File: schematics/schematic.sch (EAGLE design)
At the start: 8 parts, among them IC1 4021N, IC2 4021N

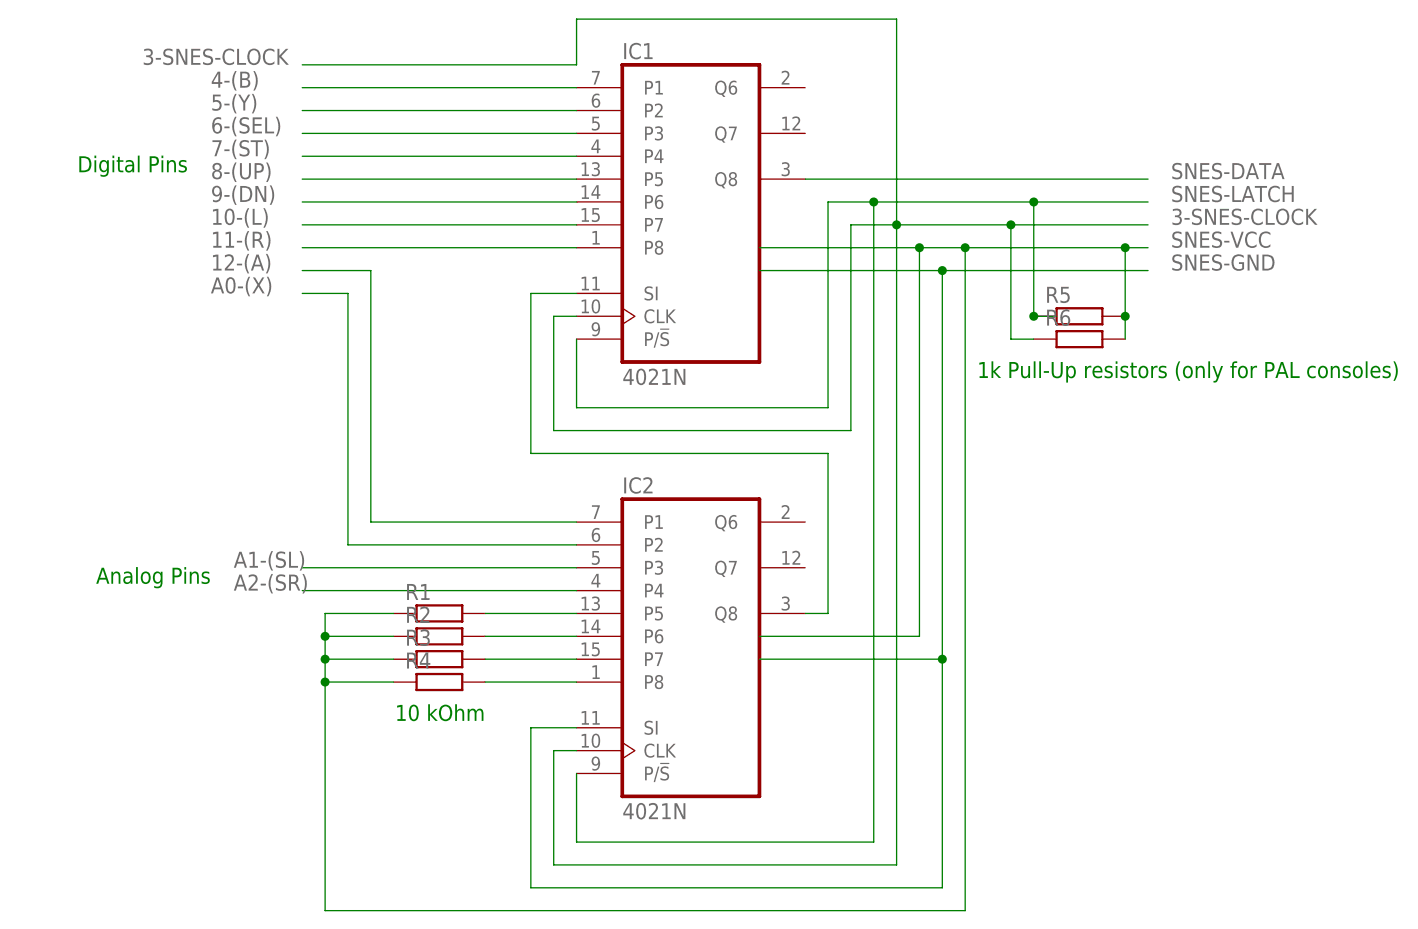
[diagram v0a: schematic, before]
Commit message: Updated schematic - connect latch to arduino
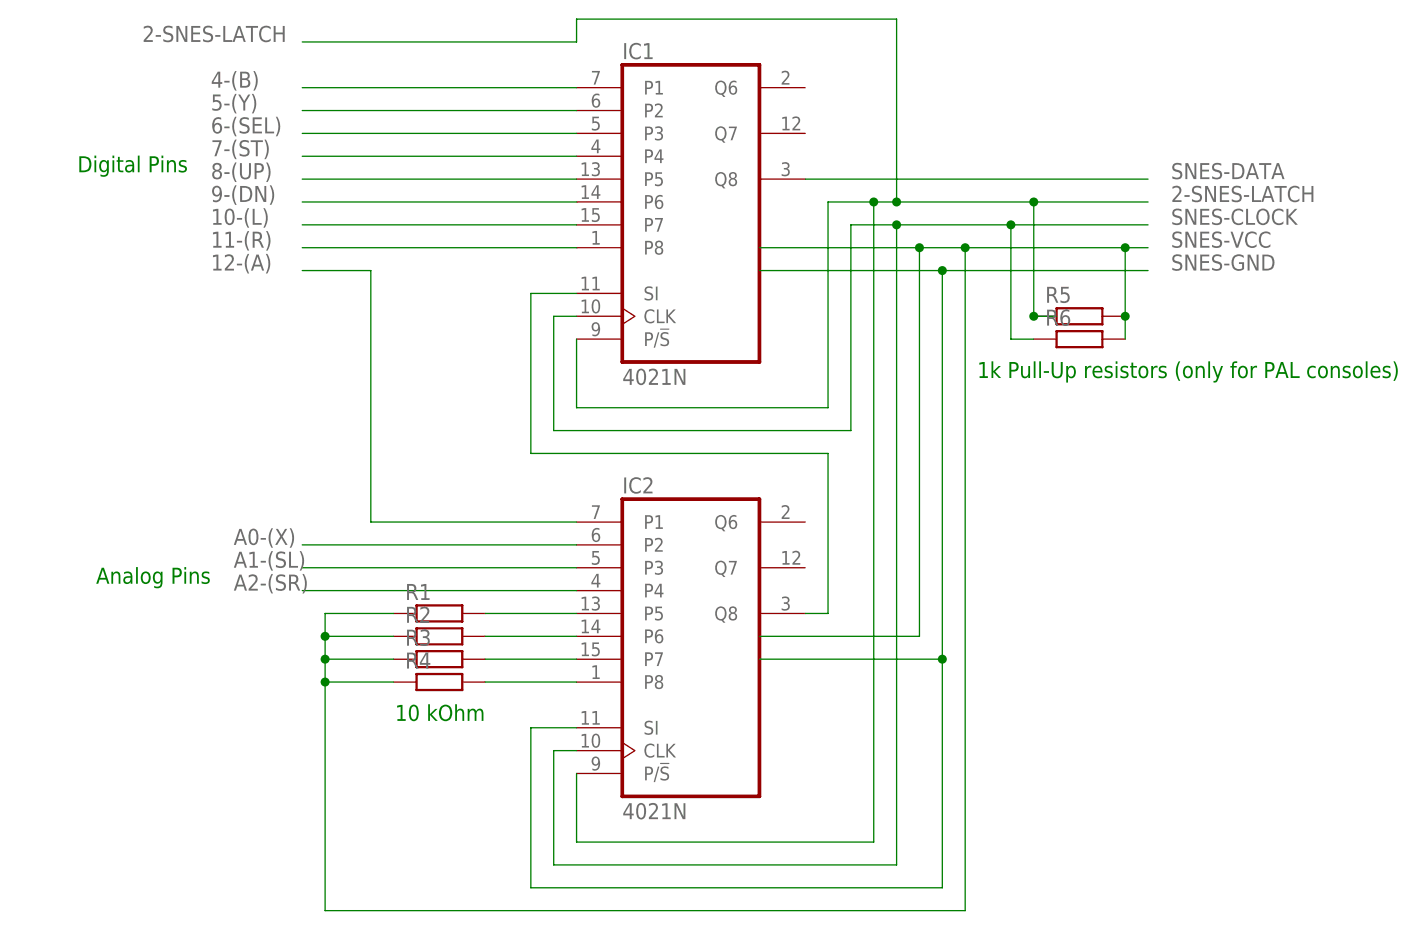
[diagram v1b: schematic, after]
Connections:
- net 3-SNES-CLOCK renamed SNES-CLOCK
- net SNES-LATCH renamed 2-SNES-LATCH
- new net A0-(X): IC2A.P2
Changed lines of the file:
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@@
-</segment>
-</net>
-<net name="A0-(X)" class="0">
-<segment>
-<wire x1="48.26" y1="30.48" x2="22.86" y2="30.48" width="0.1524" layer="91"/>
-<wire x1="22.86" y1="30.48" x2="22.86" y2="58.42" width="0.1524" layer="91"/>
-<wire x1="22.86" y1="58.42" x2="17.78" y2="58.42" width="0.1524" layer="91"/>
-<label x="7.62" y="58.42" size="1.778" layer="95"/>
 </segment>
 </net>
@@
 </segment>
 </net>
-<net name="SNES-LATCH" class="0">
+<net name="2-SNES-LATCH" class="0">
 <segment>
 <pinref part="IC1" gate="A" pin="P/!S"/>
@@
 <label x="114.3" y="68.58" size="1.778" layer="95"/>
 <pinref part="IC2" gate="A" pin="P/!S"/>
-<wire x1="81.28" y1="68.58" x2="99.06" y2="68.58" width="0.1524" layer="91"/>
+<wire x1="81.28" y1="68.58" x2="83.82" y2="68.58" width="0.1524" layer="91"/>
+<wire x1="83.82" y1="68.58" x2="99.06" y2="68.58" width="0.1524" layer="91"/>
 <wire x1="99.06" y1="68.58" x2="111.76" y2="68.58" width="0.1524" layer="91"/>
 <wire x1="48.26" y1="5.08" x2="48.26" y2="-2.54" width="0.1524" layer="91"/>
@@
 <junction x="99.06" y="55.88"/>
 <junction x="99.06" y="68.58"/>
+<label x="0" y="86.36" size="1.778" layer="95"/>
+<wire x1="83.82" y1="88.9" x2="83.82" y2="68.58" width="0.1524" layer="91"/>
+<junction x="83.82" y="68.58"/>
+<wire x1="83.82" y1="88.9" x2="48.26" y2="88.9" width="0.1524" layer="91"/>
+<wire x1="48.26" y1="88.9" x2="48.26" y2="86.36" width="0.1524" layer="91"/>
+<wire x1="48.26" y1="86.36" x2="17.78" y2="86.36" width="0.1524" layer="91"/>
 </segment>
 </net>
-<net name="3-SNES-CLOCK" class="0">
+<net name="SNES-CLOCK" class="0">
 <segment>
 <pinref part="IC1" gate="A" pin="CLK"/>
@@
 <wire x1="83.82" y1="-5.08" x2="83.82" y2="66.04" width="0.1524" layer="91"/>
 <junction x="83.82" y="66.04"/>
-<wire x1="83.82" y1="66.04" x2="83.82" y2="88.9" width="0.1524" layer="91"/>
-<wire x1="83.82" y1="88.9" x2="48.26" y2="88.9" width="0.1524" layer="91"/>
-<wire x1="48.26" y1="88.9" x2="48.26" y2="83.82" width="0.1524" layer="91"/>
-<wire x1="48.26" y1="83.82" x2="17.78" y2="83.82" width="0.1524" layer="91"/>
-<label x="0" y="83.82" size="1.778" layer="95"/>
 <pinref part="R6" gate="G$1" pin="1"/>
 <wire x1="99.06" y1="53.34" x2="96.52" y2="53.34" width="0.1524" layer="91"/>
@@
 <net name="SNES-GND" class="0">
 <segment>
+<wire x1="88.9" y1="17.78" x2="88.9" y2="60.96" width="0.1524" layer="91"/>
+<wire x1="111.76" y1="60.96" x2="88.9" y2="60.96" width="0.1524" layer="91"/>
+<wire x1="68.58" y1="60.96" x2="88.9" y2="60.96" width="0.1524" layer="91"/>
+<junction x="88.9" y="60.96"/>
+<wire x1="68.58" y1="17.78" x2="88.9" y2="17.78" width="0.1524" layer="91"/>
+<label x="114.3" y="60.96" size="1.778" layer="95"/>
 <pinref part="IC2" gate="A" pin="SI"/>
 <wire x1="48.26" y1="10.16" x2="43.18" y2="10.16" width="0.1524" layer="91"/>
@@
 <wire x1="43.18" y1="-7.62" x2="88.9" y2="-7.62" width="0.1524" layer="91"/>
 <wire x1="88.9" y1="-7.62" x2="88.9" y2="17.78" width="0.1524" layer="91"/>
-<wire x1="88.9" y1="17.78" x2="88.9" y2="60.96" width="0.1524" layer="91"/>
-<wire x1="111.76" y1="60.96" x2="88.9" y2="60.96" width="0.1524" layer="91"/>
-<wire x1="68.58" y1="60.96" x2="88.9" y2="60.96" width="0.1524" layer="91"/>
-<junction x="88.9" y="60.96"/>
-<wire x1="68.58" y1="17.78" x2="88.9" y2="17.78" width="0.1524" layer="91"/>
 <junction x="88.9" y="17.78"/>
-<label x="114.3" y="60.96" size="1.778" layer="95"/>
 </segment>
 </net>
+<net name="A0-(X)" class="0">
+<segment>
+<pinref part="IC2" gate="A" pin="P2"/>
+<wire x1="48.26" y1="30.48" x2="17.78" y2="30.48" width="0.1524" layer="91"/>
+<label x="10.16" y="30.48" size="1.778" layer="95"/>
+</segment>
+</net>

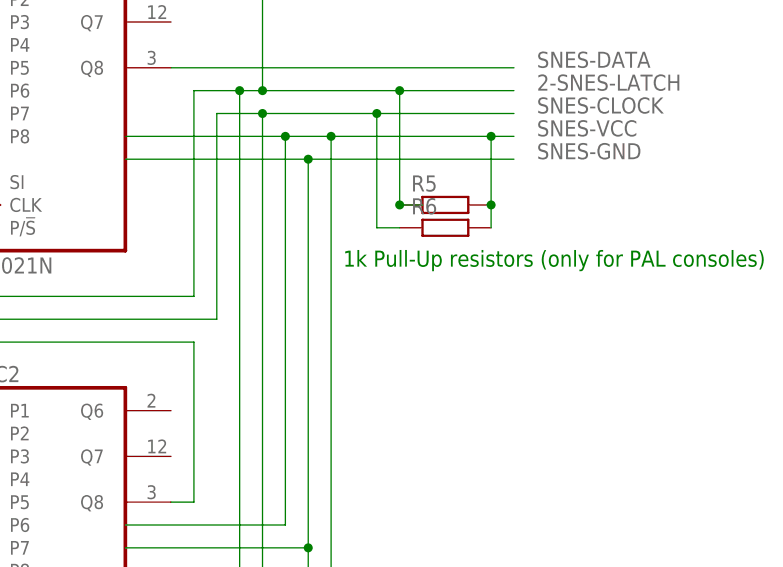
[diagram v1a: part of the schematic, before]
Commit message: Changed pull-up resistor for LATCH to 2,2kOhm
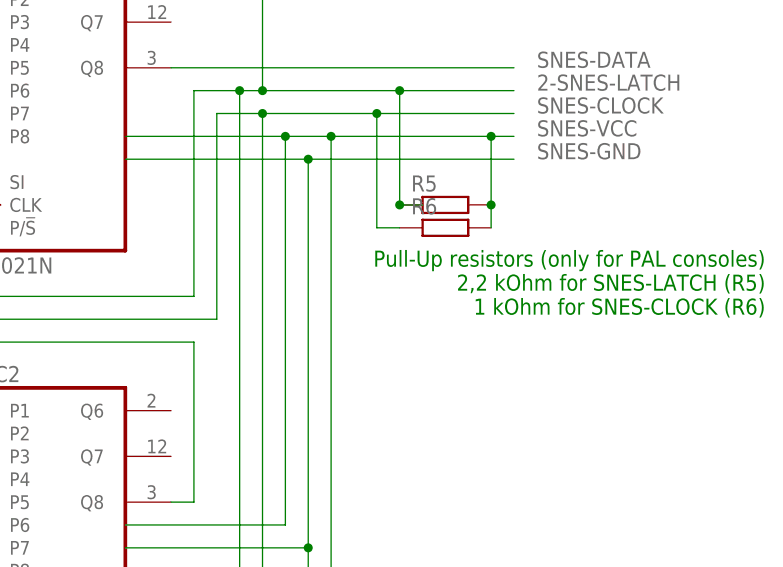
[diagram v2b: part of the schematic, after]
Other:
- note added: "Pull-Up resistors (only for PAL consoles) 2,2 kOhm for SNES-LATCH (R5) 1 kOhm for SNES-CLOCK (R6)"
- note removed: "1k Pull-Up resistors (only for PAL consoles)"
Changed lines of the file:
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@@
 <text x="7.62" y="27.94" size="1.778" layer="91" rot="R180">Analog Pins</text>
 <text x="38.1" y="12.7" size="1.778" layer="91" rot="R180">10 kOhm</text>
-<text x="139.7" y="50.8" size="1.778" layer="91" rot="R180">1k Pull-Up resistors (only for PAL consoles)</text>
+<text x="139.7" y="50.8" size="1.778" layer="91" rot="R180">Pull-Up resistors (only for PAL consoles)
+2,2 kOhm for SNES-LATCH (R5)
+1 kOhm for SNES-CLOCK (R6)</text>
 </plain>
 <instances>
@@
 </drawing>
 <compatibility>
+<note version="6.3" minversion="6.2.2" severity="warning">
+Since Version 6.2.2 text objects can contain more than one line,
+which will not be processed correctly with this version.
+</note>
 <note version="8.2" severity="warning">
 Since Version 8.2, EAGLE supports online libraries. The ids
